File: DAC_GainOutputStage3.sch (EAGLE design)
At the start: 55 parts, among them J1 1935190, J3 SJ-63033A

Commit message: Finished schematic and working layout
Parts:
- removed C10O: 0.1uF, 35V, Dual Mono Amp Library:MKS4B031002A00JC00
- removed C7O: 30uF/400V, Dual Mono Amp Library:DCP4G053006ID2KSSD
- removed R7O: 1M*, Dual Mono Amp Library:LR1F1M0
- added C21O1: 30uF/400V, Dual Mono Amp Library:DCP4G053006ID2KSSD
- added C2O1: 0.1uF, 35V, Dual Mono Amp Library:MKS4B031002A00JC00
- added D4, D5, D6: (no value), adafruit:DIODEDO-1N4148
- added R10, R16: 48.7, rcl:R-US_0207/10
- added R11, R12: 9.1k, rcl:R-US_0207/10
- added R13, R14: 1k, rcl:R-US_0207/10
- added R15: 330, rcl:R-US_0207/10
- added R3O1: 1M*, Dual Mono Amp Library:LR1F1M0
- added U1, U2: V_REG_317SMD, SparkFun-IC-Power:V_REG_317SMD
- added Z1, Z2: 1N750, 1N750:1N750
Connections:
- new net N$29: D6.A, R13.1, SX2.7
- new net N$37: R10.2, U1.OUT
- new net N$38: R16.2, U2.OUT
- net +240VDC: now also C2O1.1, R11.2, R12.2, SX2.9; no longer SX2.6
- net AGND: now also R10.1, R15.1, R16.1, R3O1.2, U1.ADJ, U2.ADJ; no longer C10O.2, R7O.2
- net L+: now also R4.2; no longer R4.1
- net L-: now also R3.2; no longer R3.1
- net L_OUT: now also C21O1.1; no longer C7O.1, R7O.1
- net N$14: now also R14.1, SX2.2, Z2.A; no longer R3.2, SX4.2
- net N$17: now also C2O1.2, R14.2, R3O1.1; no longer R4.2, SX4.7
- net N$2: now also Z1.A
- net N$22: now also U1.IN
- net N$26: now also Z1.K
- net N$27: now also R15.2, SX2.3, Z2.K; no longer SX4.3, SX4.6
- net N$3: now also C21O1.2, D6.C, SX2.1, SX2.6; no longer SX2.7
- net N$4: now also D4.A, R3.1, SX4.2; no longer SX2.8
- net N$5: now also D5.A, R4.1, SX4.7; no longer C7O.2, SX2.1
- net N$7: now also D4.C, D5.C, SX4.3, SX4.6, U2.IN; no longer SX2.2
- net N$8: now also R11.1, SX4.1; no longer SX2.3
- net N$9: now also R12.1, R13.2, SX4.9; no longer C10O.1, SX2.9
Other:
- moved on the sheet: C11O, C12O, C13O, C14O, C15O, C2, C21O, C24O, C25O, C26O, C2O, C4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

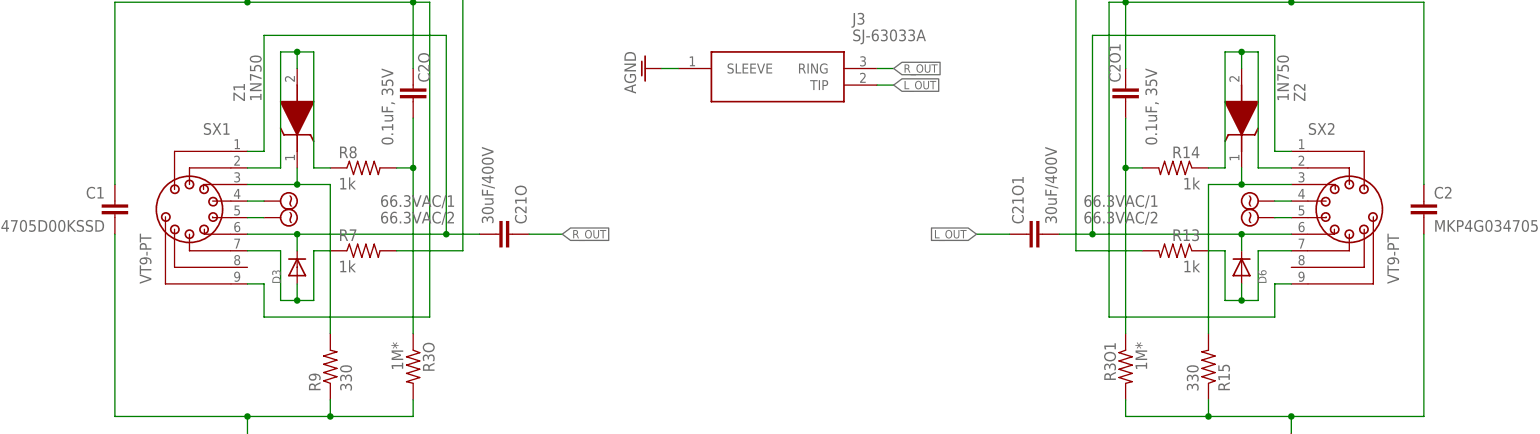
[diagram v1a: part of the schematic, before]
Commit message: Fixed schematic
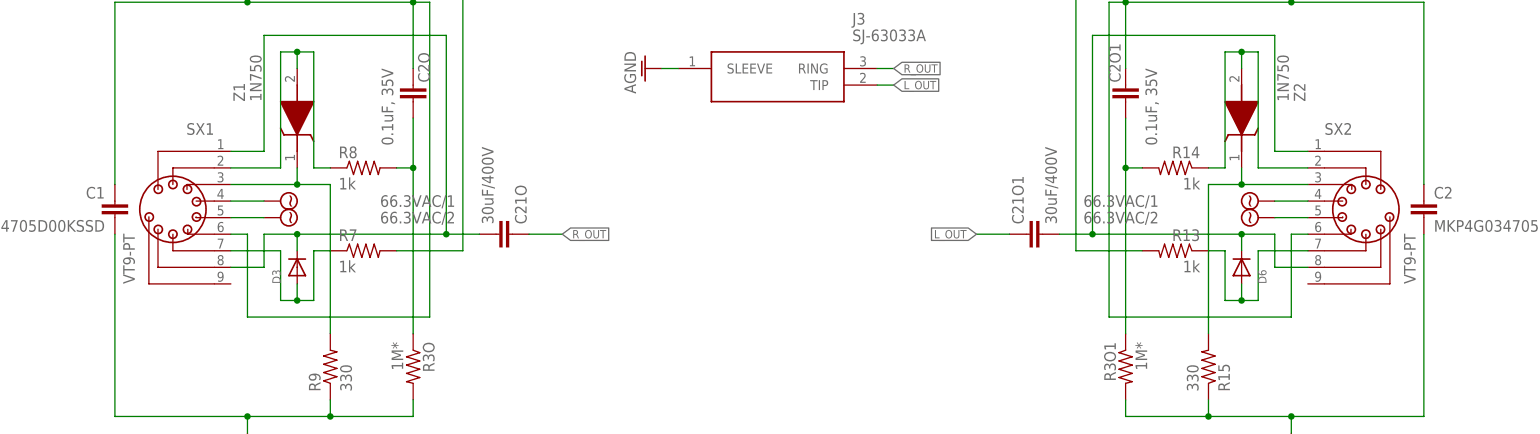
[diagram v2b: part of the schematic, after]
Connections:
- net +240VDC: now also SX1.6, SX2.6; no longer SX1.9, SX2.9
- net N$18: now also SX1.8; no longer SX1.6
- net N$3: now also SX2.8; no longer SX2.6
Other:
- moved on the sheet: SX1, SX2
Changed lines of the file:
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@@
 <attribute name="VALUE" x="91.44" y="209.55" size="1.778" layer="96" rot="R90" align="center-left"/>
 </instance>
-<instance part="SX1" gate="G$1" x="12.7" y="124.46" smashed="yes" rot="MR0">
-<attribute name="NAME" x="17.78" y="137.16" size="1.778" layer="95" rot="MR0"/>
-<attribute name="VALUE" x="3.81" y="114.3" size="1.778" layer="96" rot="MR90"/>
+<instance part="SX1" gate="G$1" x="10.16" y="124.46" smashed="yes" rot="MR0">
+<attribute name="NAME" x="15.24" y="137.16" size="1.778" layer="95" rot="MR0"/>
+<attribute name="VALUE" x="1.27" y="114.3" size="1.778" layer="96" rot="MR90"/>
 </instance>
 <instance part="U$8" gate="G$1" x="20.32" y="162.56" smashed="yes" rot="MR0">
@@
 <attribute name="VALUE" x="63.246" y="169.418" size="1.778" layer="96"/>
 </instance>
-<instance part="SX2" gate="G$1" x="187.96" y="124.46" smashed="yes">
-<attribute name="NAME" x="182.88" y="137.16" size="1.778" layer="95"/>
-<attribute name="VALUE" x="196.85" y="114.3" size="1.778" layer="96" rot="R90"/>
+<instance part="SX2" gate="G$1" x="190.5" y="124.46" smashed="yes">
+<attribute name="NAME" x="185.42" y="137.16" size="1.778" layer="95"/>
+<attribute name="VALUE" x="199.39" y="114.3" size="1.778" layer="96" rot="R90"/>
 </instance>
 <instance part="U$3" gate="G$1" x="180.34" y="162.56" smashed="yes">
@@
 <junction x="20.32" y="157.48"/>
 <wire x1="48.26" y1="157.48" x2="45.72" y2="157.48" width="0.1524" layer="91"/>
-<pinref part="SX1" gate="G$1" pin="9"/>
 <wire x1="45.72" y1="157.48" x2="20.32" y2="157.48" width="0.1524" layer="91"/>
 <wire x1="48.26" y1="157.48" x2="48.26" y2="109.22" width="0.1524" layer="91"/>
-<wire x1="48.26" y1="109.22" x2="22.86" y2="109.22" width="0.1524" layer="91"/>
-<wire x1="22.86" y1="109.22" x2="22.86" y2="114.3" width="0.1524" layer="91"/>
-<wire x1="22.86" y1="114.3" x2="20.32" y2="114.3" width="0.1524" layer="91"/>
+<wire x1="48.26" y1="109.22" x2="20.32" y2="109.22" width="0.1524" layer="91"/>
 <pinref part="C2O" gate="G$1" pin="1"/>
 <wire x1="45.72" y1="147.32" x2="45.72" y2="157.48" width="0.1524" layer="91"/>
@@
 <pinref part="C1" gate="G$1" pin="1"/>
 <wire x1="0" y1="157.48" x2="0" y2="129.54" width="0.1524" layer="91"/>
+<pinref part="SX1" gate="G$1" pin="6"/>
+<wire x1="17.78" y1="121.92" x2="20.32" y2="121.92" width="0.1524" layer="91"/>
+<wire x1="20.32" y1="121.92" x2="20.32" y2="109.22" width="0.1524" layer="91"/>
 </segment>
 <segment>
@@
 <junction x="180.34" y="157.48"/>
 <wire x1="152.4" y1="157.48" x2="154.94" y2="157.48" width="0.1524" layer="91"/>
-<pinref part="SX2" gate="G$1" pin="9"/>
 <wire x1="154.94" y1="157.48" x2="180.34" y2="157.48" width="0.1524" layer="91"/>
 <wire x1="152.4" y1="157.48" x2="152.4" y2="109.22" width="0.1524" layer="91"/>
-<wire x1="152.4" y1="109.22" x2="177.8" y2="109.22" width="0.1524" layer="91"/>
-<wire x1="177.8" y1="109.22" x2="177.8" y2="114.3" width="0.1524" layer="91"/>
-<wire x1="177.8" y1="114.3" x2="180.34" y2="114.3" width="0.1524" layer="91"/>
+<wire x1="152.4" y1="109.22" x2="180.34" y2="109.22" width="0.1524" layer="91"/>
 <pinref part="C2O1" gate="G$1" pin="1"/>
 <wire x1="154.94" y1="147.32" x2="154.94" y2="157.48" width="0.1524" layer="91"/>
@@
 <pinref part="C2" gate="G$1" pin="1"/>
 <wire x1="200.66" y1="157.48" x2="200.66" y2="129.54" width="0.1524" layer="91"/>
+<wire x1="180.34" y1="109.22" x2="180.34" y2="121.92" width="0.1524" layer="91"/>
+<pinref part="SX2" gate="G$1" pin="6"/>
+<wire x1="180.34" y1="121.92" x2="182.88" y2="121.92" width="0.1524" layer="91"/>
 </segment>
 <segment>
@@
 <pinref part="SX1" gate="G$1" pin="4"/>
 <pinref part="U$9" gate="G$1" pin="66.3VAC/1"/>
-<wire x1="22.86" y1="127" x2="20.32" y2="127" width="0.1524" layer="91"/>
+<wire x1="22.86" y1="127" x2="17.78" y2="127" width="0.1524" layer="91"/>
 </segment>
 <segment>
@@
 <pinref part="SX2" gate="G$1" pin="4"/>
 <pinref part="U$4" gate="G$1" pin="66.3VAC/1"/>
-<wire x1="177.8" y1="127" x2="180.34" y2="127" width="0.1524" layer="91"/>
+<wire x1="177.8" y1="127" x2="182.88" y2="127" width="0.1524" layer="91"/>
 </segment>
 <segment>
@@
 <pinref part="SX1" gate="G$1" pin="5"/>
 <pinref part="U$10" gate="G$1" pin="66.3VAC/2"/>
-<wire x1="22.86" y1="124.46" x2="20.32" y2="124.46" width="0.1524" layer="91"/>
+<wire x1="22.86" y1="124.46" x2="17.78" y2="124.46" width="0.1524" layer="91"/>
 </segment>
 <segment>
@@
 <pinref part="SX2" gate="G$1" pin="5"/>
 <pinref part="U$7" gate="G$1" pin="66.3VAC/2"/>
-<wire x1="177.8" y1="124.46" x2="180.34" y2="124.46" width="0.1524" layer="91"/>
+<wire x1="177.8" y1="124.46" x2="182.88" y2="124.46" width="0.1524" layer="91"/>
 </segment>
 <segment>
@@
 <pinref part="C21O" gate="G$1" pin="2"/>
 <pinref part="SX1" gate="G$1" pin="1"/>
-<wire x1="20.32" y1="134.62" x2="22.86" y2="134.62" width="0.1524" layer="91"/>
+<wire x1="17.78" y1="134.62" x2="22.86" y2="134.62" width="0.1524" layer="91"/>
 <wire x1="22.86" y1="134.62" x2="22.86" y2="152.4" width="0.1524" layer="91"/>
 <wire x1="22.86" y1="152.4" x2="50.8" y2="152.4" width="0.1524" layer="91"/>
 <wire x1="50.8" y1="152.4" x2="50.8" y2="121.92" width="0.1524" layer="91"/>
-<pinref part="SX1" gate="G$1" pin="6"/>
 <wire x1="50.8" y1="121.92" x2="27.94" y2="121.92" width="0.1524" layer="91"/>
-<wire x1="27.94" y1="121.92" x2="20.32" y2="121.92" width="0.1524" layer="91"/>
 <wire x1="55.88" y1="121.92" x2="50.8" y2="121.92" width="0.1524" layer="91"/>
 <junction x="50.8" y="121.92"/>
 <pinref part="D3" gate="G$1" pin="C"/>
 <wire x1="27.94" y1="119.38" x2="27.94" y2="121.92" width="0.1524" layer="91"/>
+<pinref part="SX1" gate="G$1" pin="8"/>
+<wire x1="17.78" y1="116.84" x2="22.86" y2="116.84" width="0.1524" layer="91"/>
+<wire x1="22.86" y1="116.84" x2="22.86" y2="121.92" width="0.1524" layer="91"/>
+<wire x1="22.86" y1="121.92" x2="27.94" y2="121.92" width="0.1524" layer="91"/>
 <junction x="27.94" y="121.92"/>
 </segment>
@@
 <wire x1="27.94" y1="149.86" x2="25.4" y2="149.86" width="0.1524" layer="91"/>
 <wire x1="25.4" y1="149.86" x2="25.4" y2="132.08" width="0.1524" layer="91"/>
-<wire x1="25.4" y1="132.08" x2="20.32" y2="132.08" width="0.1524" layer="91"/>
+<wire x1="25.4" y1="132.08" x2="17.78" y2="132.08" width="0.1524" layer="91"/>
 <pinref part="Z1" gate="G$1" pin="A"/>
 <wire x1="27.94" y1="147.32" x2="27.94" y2="149.86" width="0.1524" layer="91"/>
@@
 <segment>
 <pinref part="SX1" gate="G$1" pin="3"/>
-<wire x1="20.32" y1="129.54" x2="27.94" y2="129.54" width="0.1524" layer="91"/>
+<wire x1="17.78" y1="129.54" x2="27.94" y2="129.54" width="0.1524" layer="91"/>
 <pinref part="R9" gate="G$1" pin="2"/>
 <wire x1="27.94" y1="129.54" x2="33.02" y2="129.54" width="0.1524" layer="91"/>
@@
 <wire x1="27.94" y1="111.76" x2="25.4" y2="111.76" width="0.1524" layer="91"/>
 <wire x1="25.4" y1="111.76" x2="25.4" y2="119.38" width="0.1524" layer="91"/>
-<wire x1="25.4" y1="119.38" x2="20.32" y2="119.38" width="0.1524" layer="91"/>
+<wire x1="25.4" y1="119.38" x2="17.78" y2="119.38" width="0.1524" layer="91"/>
 <pinref part="D3" gate="G$1" pin="A"/>
 <wire x1="27.94" y1="114.3" x2="27.94" y2="111.76" width="0.1524" layer="91"/>
@@
 <pinref part="C21O1" gate="G$1" pin="2"/>
 <pinref part="SX2" gate="G$1" pin="1"/>
-<wire x1="180.34" y1="134.62" x2="177.8" y2="134.62" width="0.1524" layer="91"/>
+<wire x1="182.88" y1="134.62" x2="177.8" y2="134.62" width="0.1524" layer="91"/>
 <wire x1="177.8" y1="134.62" x2="177.8" y2="152.4" width="0.1524" layer="91"/>
 <wire x1="177.8" y1="152.4" x2="149.86" y2="152.4" width="0.1524" layer="91"/>
 <wire x1="149.86" y1="152.4" x2="149.86" y2="121.92" width="0.1524" layer="91"/>
-<pinref part="SX2" gate="G$1" pin="6"/>
 <wire x1="149.86" y1="121.92" x2="172.72" y2="121.92" width="0.1524" layer="91"/>
-<wire x1="172.72" y1="121.92" x2="180.34" y2="121.92" width="0.1524" layer="91"/>
 <wire x1="144.78" y1="121.92" x2="149.86" y2="121.92" width="0.1524" layer="91"/>
 <junction x="149.86" y="121.92"/>
 <pinref part="D6" gate="G$1" pin="C"/>
 <wire x1="172.72" y1="119.38" x2="172.72" y2="121.92" width="0.1524" layer="91"/>
+<wire x1="172.72" y1="121.92" x2="177.8" y2="121.92" width="0.1524" layer="91"/>
 <junction x="172.72" y="121.92"/>
+<wire x1="177.8" y1="121.92" x2="177.8" y2="116.84" width="0.1524" layer="91"/>
+<pinref part="SX2" gate="G$1" pin="8"/>
+<wire x1="177.8" y1="116.84" x2="182.88" y2="116.84" width="0.1524" layer="91"/>
 </segment>
 </net>
@@
 <wire x1="172.72" y1="149.86" x2="175.26" y2="149.86" width="0.1524" layer="91"/>
 <wire x1="175.26" y1="149.86" x2="175.26" y2="132.08" width="0.1524" layer="91"/>
-<wire x1="175.26" y1="132.08" x2="180.34" y2="132.08" width="0.1524" layer="91"/>
+<wire x1="175.26" y1="132.08" x2="182.88" y2="132.08" width="0.1524" layer="91"/>
 <pinref part="Z2" gate="G$1" pin="A"/>
 <wire x1="172.72" y1="147.32" x2="172.72" y2="149.86" width="0.1524" layer="91"/>
@@
 <segment>
 <pinref part="SX2" gate="G$1" pin="3"/>
-<wire x1="180.34" y1="129.54" x2="172.72" y2="129.54" width="0.1524" layer="91"/>
+<wire x1="182.88" y1="129.54" x2="172.72" y2="129.54" width="0.1524" layer="91"/>
 <pinref part="R15" gate="G$1" pin="2"/>
 <wire x1="172.72" y1="129.54" x2="167.64" y2="129.54" width="0.1524" layer="91"/>
@@
 <wire x1="172.72" y1="111.76" x2="175.26" y2="111.76" width="0.1524" layer="91"/>
 <wire x1="175.26" y1="111.76" x2="175.26" y2="119.38" width="0.1524" layer="91"/>
-<wire x1="175.26" y1="119.38" x2="180.34" y2="119.38" width="0.1524" layer="91"/>
+<wire x1="175.26" y1="119.38" x2="182.88" y2="119.38" width="0.1524" layer="91"/>
 <pinref part="D6" gate="G$1" pin="A"/>
 <wire x1="172.72" y1="114.3" x2="172.72" y2="111.76" width="0.1524" layer="91"/>

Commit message: Finished routing
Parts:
- removed SH1: SHORTA5, Dual Mono Amp Library:SHORTA5
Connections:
- removed net DGND: J1.4, SH1.P$1
- net AGND: now also J1.4; no longer SH1.P$2
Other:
- moved on the sheet: C1, C2, D3, D6, R15, R9, SX1, SX2, Z1, Z2

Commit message: Progress
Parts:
- removed Z1, Z2: 1N750, 1N750:1N750
- added Z3, Z4: 1N750, Dual Mono Amp Library:1N750
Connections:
- net N$14: now also Z4.A; no longer Z2.A
- net N$2: now also Z3.A; no longer Z1.A
- net N$26: now also Z3.C; no longer Z1.K
- net N$27: now also Z4.C; no longer Z2.K
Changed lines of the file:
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@@
 <part name="D2" library="adafruit" library_urn="urn:adsk.eagle:library:420" deviceset="DIODE" device="DO-1N4148" package3d_urn="urn:adsk.eagle:package:6240748/1"/>
 <part name="D3" library="adafruit" library_urn="urn:adsk.eagle:library:420" deviceset="DIODE" device="DO-1N4148" package3d_urn="urn:adsk.eagle:package:6240748/1"/>
-<part name="Z1" library="1N750" deviceset="1N750" device=""/>
 <part name="U1" library="SparkFun-IC-Power" library_urn="urn:adsk.eagle:library:526" deviceset="V_REG_317" device="SMD" package3d_urn="urn:adsk.eagle:package:39069/2"/>
 <part name="R10" library="rcl" library_urn="urn:adsk.eagle:library:334" deviceset="R-US_" device="0207/10" package3d_urn="urn:adsk.eagle:package:23491/2" value="48.7"/>
@@
 <part name="D5" library="adafruit" library_urn="urn:adsk.eagle:library:420" deviceset="DIODE" device="DO-1N4148" package3d_urn="urn:adsk.eagle:package:6240748/1"/>
 <part name="D6" library="adafruit" library_urn="urn:adsk.eagle:library:420" deviceset="DIODE" device="DO-1N4148" package3d_urn="urn:adsk.eagle:package:6240748/1"/>
-<part name="Z2" library="1N750" deviceset="1N750" device=""/>
 <part name="U2" library="SparkFun-IC-Power" library_urn="urn:adsk.eagle:library:526" deviceset="V_REG_317" device="SMD" package3d_urn="urn:adsk.eagle:package:39069/2"/>
 <part name="R16" library="rcl" library_urn="urn:adsk.eagle:library:334" deviceset="R-US_" device="0207/10" package3d_urn="urn:adsk.eagle:package:23491/2" value="48.7"/>
 <part name="AGND19" library="Dual Mono Amp Library" library_urn="urn:adsk.wipprod:fs.file:vf.VjdQUjkvQKmMNRW9J90YWw" deviceset="AGND" device=""/>
+<part name="Z3" library="Dual Mono Amp Library" library_urn="urn:adsk.eagle:library:47621477" deviceset="1N750" device="" package3d_urn="urn:adsk.eagle:package:48500160/1"/>
+<part name="Z4" library="Dual Mono Amp Library" library_urn="urn:adsk.eagle:library:47621477" deviceset="1N750" device="" package3d_urn="urn:adsk.eagle:package:48500160/1"/>
 </parts>
 <sheets>
@@
 <attribute name="VALUE" x="29.21" y="114.3" size="1.27" layer="96" rot="R90"/>
 </instance>
-<instance part="Z1" gate="G$1" x="25.4" y="132.08" smashed="yes" rot="R90">
-<attribute name="NAME" x="16.51" y="142.24" size="1.778" layer="95" rot="R90" align="center-left"/>
-<attribute name="VALUE" x="19.05" y="142.24" size="1.778" layer="96" rot="R90" align="center-left"/>
-</instance>
 <instance part="U1" gate="G$1" x="60.96" y="193.04" smashed="yes">
 <attribute name="NAME" x="63.5" y="185.42" size="1.778" layer="95"/>
@@
 <attribute name="VALUE" x="171.45" y="114.3" size="1.27" layer="96" rot="MR90"/>
 </instance>
-<instance part="Z2" gate="G$1" x="175.26" y="132.08" smashed="yes" rot="MR90">
-<attribute name="NAME" x="184.15" y="142.24" size="1.778" layer="95" rot="MR90" align="center-left"/>
-<attribute name="VALUE" x="181.61" y="142.24" size="1.778" layer="96" rot="MR90" align="center-left"/>
-</instance>
 <instance part="U2" gate="G$1" x="139.7" y="193.04" smashed="yes" rot="MR0">
 <attribute name="NAME" x="137.16" y="185.42" size="1.778" layer="95" rot="MR0"/>
@@
 <instance part="AGND19" gate="VR1" x="134.62" y="172.72" smashed="yes">
 <attribute name="VALUE" x="137.414" y="169.418" size="1.778" layer="96" rot="MR0"/>
+</instance>
+<instance part="Z3" gate="G$1" x="25.4" y="134.62" smashed="yes" rot="R270">
+<attribute name="NAME" x="28.0416" y="137.5664" size="1.778" layer="95" rot="R270"/>
+<attribute name="VALUE" x="20.9042" y="139.0904" size="1.778" layer="96" rot="R270"/>
+</instance>
+<instance part="Z4" gate="G$1" x="175.26" y="134.62" smashed="yes" rot="R270">
+<attribute name="NAME" x="177.9016" y="137.5664" size="1.778" layer="95" rot="R270"/>
+<attribute name="VALUE" x="170.7642" y="139.0904" size="1.778" layer="96" rot="R270"/>
 </instance>
 </instances>
@@
 <pinref part="R8" gate="G$1" pin="1"/>
 <wire x1="33.02" y1="132.08" x2="27.94" y2="132.08" width="0.1524" layer="91"/>
-<wire x1="27.94" y1="132.08" x2="27.94" y2="149.86" width="0.1524" layer="91"/>
-<wire x1="27.94" y1="149.86" x2="25.4" y2="149.86" width="0.1524" layer="91"/>
-<wire x1="25.4" y1="149.86" x2="22.86" y2="149.86" width="0.1524" layer="91"/>
-<wire x1="22.86" y1="149.86" x2="22.86" y2="132.08" width="0.1524" layer="91"/>
+<wire x1="27.94" y1="132.08" x2="27.94" y2="139.7" width="0.1524" layer="91"/>
+<wire x1="27.94" y1="139.7" x2="25.4" y2="139.7" width="0.1524" layer="91"/>
+<wire x1="25.4" y1="139.7" x2="22.86" y2="139.7" width="0.1524" layer="91"/>
+<wire x1="22.86" y1="139.7" x2="22.86" y2="132.08" width="0.1524" layer="91"/>
 <wire x1="22.86" y1="132.08" x2="15.24" y2="132.08" width="0.1524" layer="91"/>
-<pinref part="Z1" gate="G$1" pin="A"/>
-<wire x1="25.4" y1="147.32" x2="25.4" y2="149.86" width="0.1524" layer="91"/>
-<junction x="25.4" y="149.86"/>
+<wire x1="25.4" y1="137.16" x2="25.4" y2="139.7" width="0.1524" layer="91"/>
+<junction x="25.4" y="139.7"/>
+<pinref part="Z3" gate="G$1" pin="A"/>
 </segment>
 </net>
@@
 <wire x1="25.4" y1="129.54" x2="30.48" y2="129.54" width="0.1524" layer="91"/>
 <wire x1="30.48" y1="129.54" x2="30.48" y2="106.68" width="0.1524" layer="91"/>
-<pinref part="Z1" gate="G$1" pin="K"/>
 <wire x1="25.4" y1="132.08" x2="25.4" y2="129.54" width="0.1524" layer="91"/>
 <junction x="25.4" y="129.54"/>
+<pinref part="Z3" gate="G$1" pin="C"/>
 </segment>
 </net>
@@
 <pinref part="R14" gate="G$1" pin="1"/>
 <wire x1="167.64" y1="132.08" x2="172.72" y2="132.08" width="0.1524" layer="91"/>
-<wire x1="172.72" y1="132.08" x2="172.72" y2="149.86" width="0.1524" layer="91"/>
-<wire x1="172.72" y1="149.86" x2="175.26" y2="149.86" width="0.1524" layer="91"/>
-<wire x1="175.26" y1="149.86" x2="177.8" y2="149.86" width="0.1524" layer="91"/>
-<wire x1="177.8" y1="149.86" x2="177.8" y2="132.08" width="0.1524" layer="91"/>
+<wire x1="172.72" y1="132.08" x2="172.72" y2="139.7" width="0.1524" layer="91"/>
+<wire x1="172.72" y1="139.7" x2="175.26" y2="139.7" width="0.1524" layer="91"/>
+<wire x1="175.26" y1="139.7" x2="177.8" y2="139.7" width="0.1524" layer="91"/>
+<wire x1="177.8" y1="139.7" x2="177.8" y2="132.08" width="0.1524" layer="91"/>
 <wire x1="177.8" y1="132.08" x2="185.42" y2="132.08" width="0.1524" layer="91"/>
-<pinref part="Z2" gate="G$1" pin="A"/>
-<wire x1="175.26" y1="147.32" x2="175.26" y2="149.86" width="0.1524" layer="91"/>
-<junction x="175.26" y="149.86"/>
+<wire x1="175.26" y1="137.16" x2="175.26" y2="139.7" width="0.1524" layer="91"/>
+<junction x="175.26" y="139.7"/>
+<pinref part="Z4" gate="G$1" pin="A"/>
 </segment>
 </net>
@@
 <wire x1="175.26" y1="129.54" x2="170.18" y2="129.54" width="0.1524" layer="91"/>
 <wire x1="170.18" y1="129.54" x2="170.18" y2="106.68" width="0.1524" layer="91"/>
-<pinref part="Z2" gate="G$1" pin="K"/>
 <wire x1="175.26" y1="132.08" x2="175.26" y2="129.54" width="0.1524" layer="91"/>
 <junction x="175.26" y="129.54"/>
-</segment>
-</net>
+<pinref part="Z4" gate="G$1" pin="C"/>
+</segment>
+</net>
